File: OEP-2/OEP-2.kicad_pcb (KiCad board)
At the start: 2 copper layers, 50 x 25 mm, 7 parts, among them X1 Крепеж

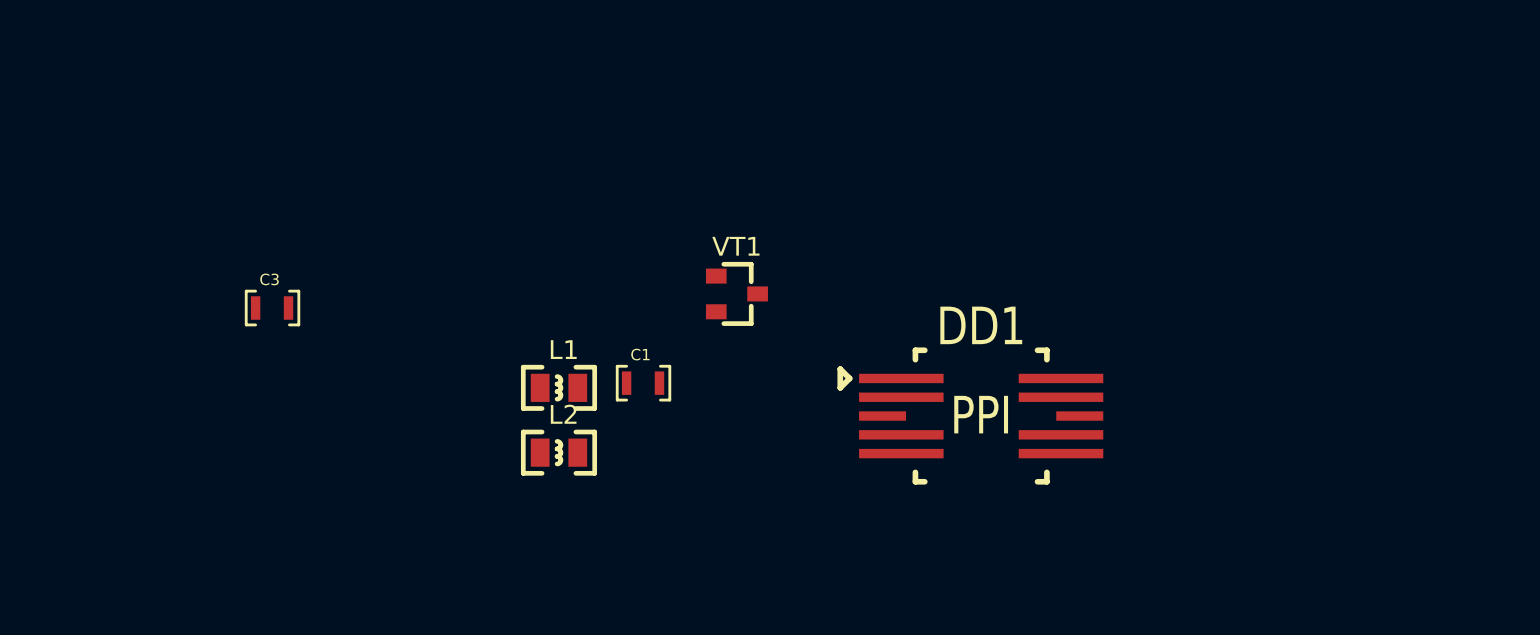
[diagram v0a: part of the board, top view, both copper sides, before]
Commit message: назначены посадочные места, кроме стабилитронов и  тантала
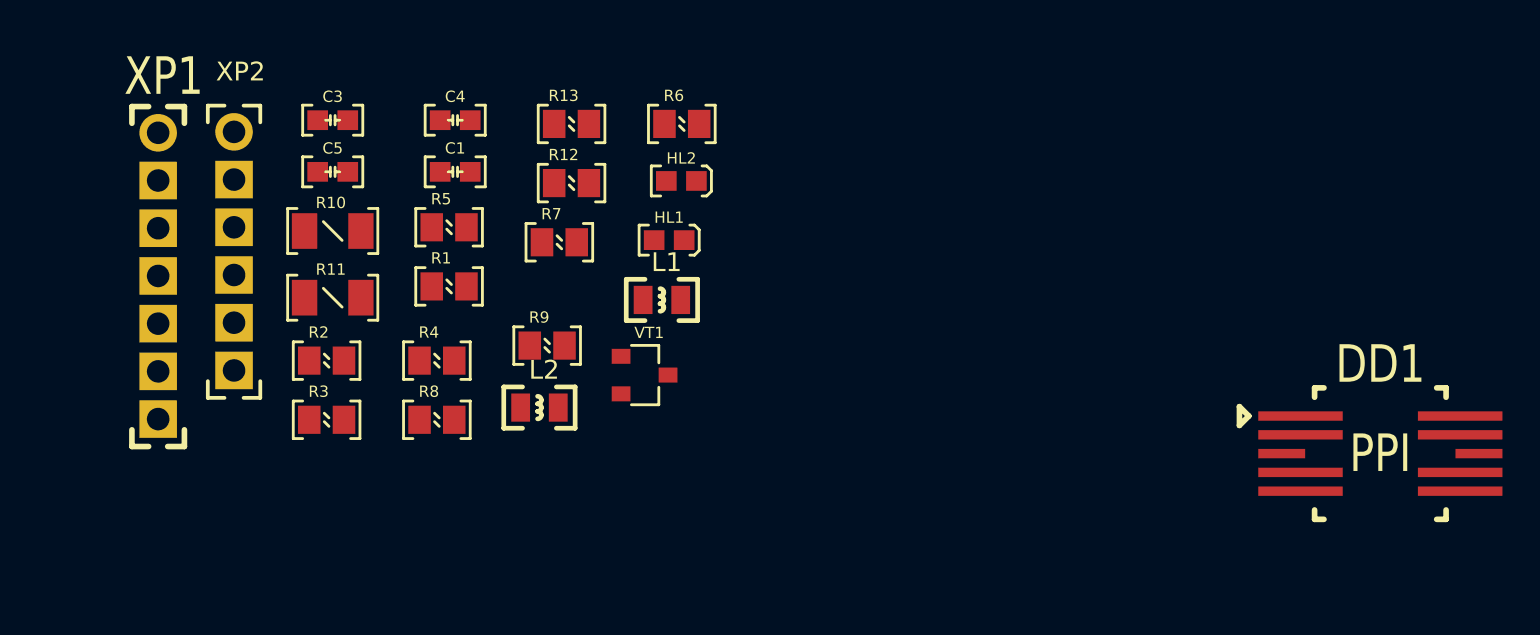
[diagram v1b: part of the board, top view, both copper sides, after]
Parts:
- added C4: Конденсатор_керамический, MOTOR_RLC:Конденсатор_SMD_IEC_0603, F.Cu at (103.8, 17.8)
- added C5: Конденсатор_керамический, MOTOR_RLC:Конденсатор_SMD_IEC_0603, F.Cu at (97.2, 20.5)
- added HL1: Светодиод, MOTOR_VD_VT_HL:Светодиод_SMD_IEC_0603, F.Cu at (115.1, 24.1)
- added HL2: Светодиод, MOTOR_VD_VT_HL:Светодиод_SMD_IEC_0603, F.Cu at (115.8, 21.0)
- added R1: Резистор_0,125Вт, MOTOR_RLC:Резистор_SMD_IEC_0805_0,125_Вт, F.Cu at (102.5, 26.6)
- added R10: Резистор_0,25Вт, MOTOR_RLC:Резистор_SMD_IEC_1206-0,25_Вт, F.Cu at (95.7, 23.6)
- added R11: Резистор_0,25Вт, MOTOR_RLC:Резистор_SMD_IEC_1206-0,25_Вт, F.Cu at (95.7, 27.2)
- added R12: Резистор_0,125Вт, MOTOR_RLC:Резистор_SMD_IEC_0805_0,125_Вт, F.Cu at (109.0, 21.1)
- added R13: Резистор_0,125Вт, MOTOR_RLC:Резистор_SMD_IEC_0805_0,125_Вт, F.Cu at (109.0, 17.9)
- added R2: Резистор_0,125Вт, MOTOR_RLC:Резистор_SMD_IEC_0805_0,125_Вт, F.Cu at (96.0, 30.6)
- added R3: Резистор_0,125Вт, MOTOR_RLC:Резистор_SMD_IEC_0805_0,125_Вт, F.Cu at (96.0, 33.7)
- added R4: Резистор_0,125Вт, MOTOR_RLC:Резистор_SMD_IEC_0805_0,125_Вт, F.Cu at (101.8, 30.6)
- added R5: Резистор_0,125Вт, MOTOR_RLC:Резистор_SMD_IEC_0805_0,125_Вт, F.Cu at (102.5, 23.4)
- added R6: Резистор_0,125Вт, MOTOR_RLC:Резистор_SMD_IEC_0805_0,125_Вт, F.Cu at (114.9, 17.9)
- added R7: Резистор_0,125Вт, MOTOR_RLC:Резистор_SMD_IEC_0805_0,125_Вт, F.Cu at (108.4, 24.2)
- added R8: Резистор_0,125Вт, MOTOR_RLC:Резистор_SMD_IEC_0805_0,125_Вт, F.Cu at (101.8, 33.7)
- added R9: Резистор_0,125Вт, MOTOR_RLC:Резистор_SMD_IEC_0805_0,125_Вт, F.Cu at (107.7, 29.8)
- added XP1: Вилка_СНП346-7ВП21-1#0, MOTOR_X:Вилка_СНП346-7ВП21-1-В, F.Cu at (87.9, 18.4)
- added XP2: Вилка_СНП346-6ВП21-1#1N1N6, MOTOR_X:Вилка_СНП346-6ВП21-1-В, F.Cu at (92.0, 18.4)
- C1, C3: footprint N_RLC:Конденсатор_SMD_0603_pnp -> MOTOR_RLC:Конденсатор_SMD_IEC_0603
- VT1: footprint N_VD_HL:Транзистор_IRLML6344TR_SOT-23 -> MOTOR_VD_VT_HL:Корпус_КТ-46
- moved DD1 21.3 mm to (151.0, 39.0)
- moved C1 15.1 mm to (103.8, 20.5)
- moved C3 10.5 mm to (97.2, 17.8)
- moved L1 7.21 mm to (113.8, 27.3)
- moved VT1 6.55 mm to (113.8, 31.3)
- moved L2 2.62 mm to (107.2, 33.0)
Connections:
- C3 pad 2: (no net) -> Net-(C3-Pad2)
- DD1 pad 1: (no net) -> /RX-RS
- DD1 pad 4: (no net) -> /TX-RS
- DD1 pad 7: (no net) -> /RS-B
- L1 pad 2: (no net) -> Net-(L1-Pad2)
- L2 pad 2: (no net) -> Net-(L2-Pad2)
- VT1 pad 1: (no net) -> Net-(R7-Pad1)
- X1 pad 1: (no net) -> Net-(X1-Pad1)

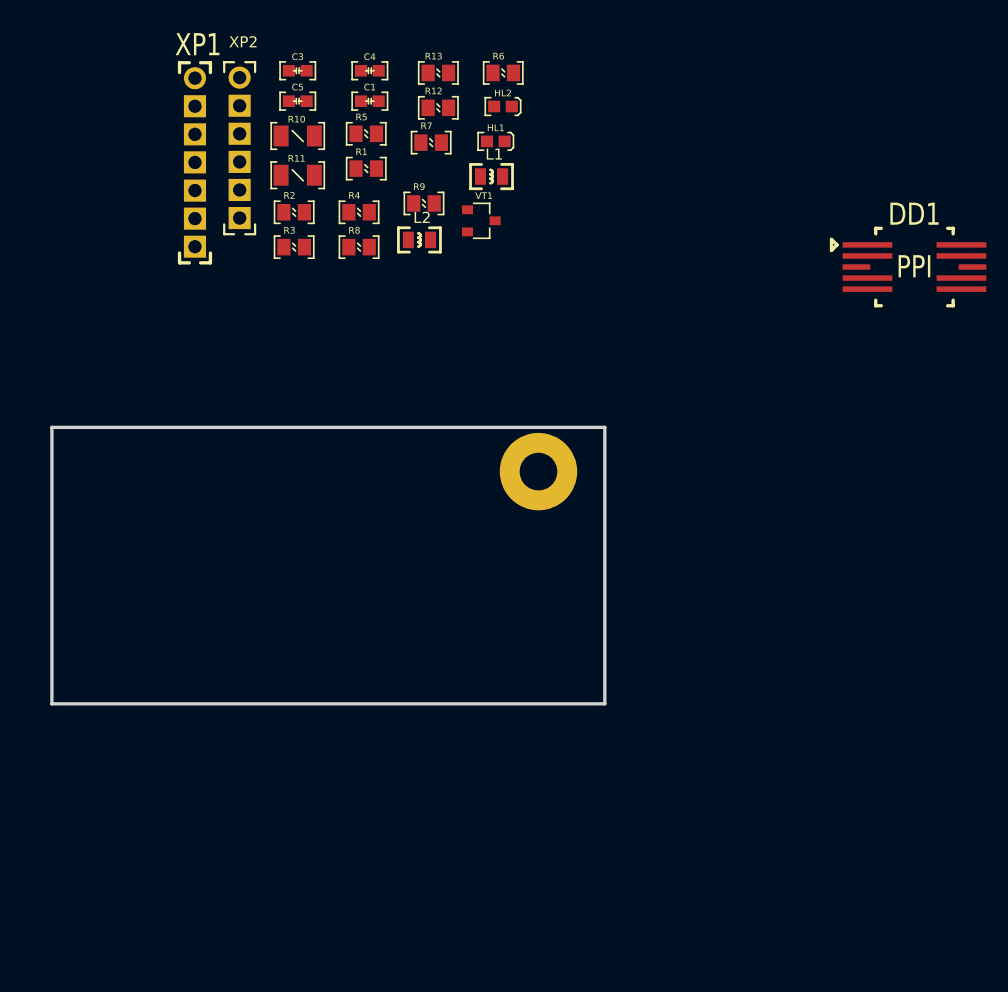
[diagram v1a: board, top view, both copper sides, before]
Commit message: назначены все посадочные места, готов сегмент  линий RS
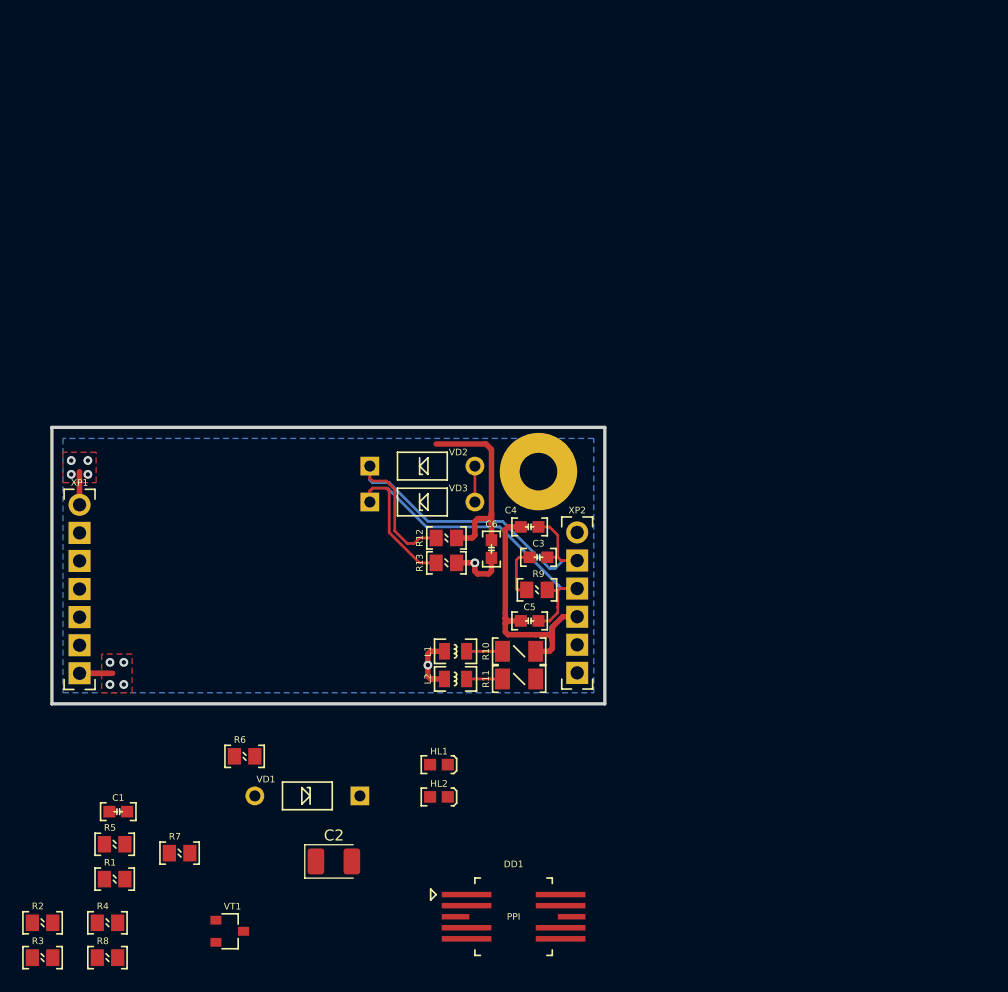
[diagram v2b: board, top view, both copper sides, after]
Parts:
- added C2: Конденсатор_электролитический, Capacitor_Tantalum_SMD:CP_EIA-3528-21_Kemet-B_Pad1.50x2.35mm_HandSolder, F.Cu at (100.5, 89.2)
- added C6: Конденсатор_керамический, N_RLC:Конденсатор_SMD_IEC_0603, F.Cu at (114.8, 61.0)
- added VD1: Стабилитрон_КС168В2, N_VD_HL:Стабилитрон_корпус_КД-2_в_отверстие, F.Cu at (93.3, 83.3)
- added VD2: Стабилитрон_КС168В2, N_VD_HL:Стабилитрон_корпус_КД-2_в_отверстие, F.Cu at (113.2, 53.5)
- added VD3: Стабилитрон_КС168В2, N_VD_HL:Стабилитрон_корпус_КД-2_в_отверстие, F.Cu at (113.2, 56.8)
- C1, C3, C4, C5: footprint MOTOR_RLC:Конденсатор_SMD_IEC_0603 -> N_RLC:Конденсатор_SMD_IEC_0603
- HL1, HL2: footprint MOTOR_VD_VT_HL:Светодиод_SMD_IEC_0603 -> N_VD_HL:Светодиод_SMD_IEC_0603
- moved DD1 69.0 mm to (114.8, 97.8)
- moved C1 68.2 mm to (81.0, 84.8)
- moved R1 68.2 mm to (79.8, 90.8)
- moved R2 68.2 mm to (73.2, 94.8)
- moved R3 68.2 mm to (73.2, 98.0)
- moved R4 68.2 mm to (79.1, 94.8)
- moved R5 68.2 mm to (79.8, 87.7)
- moved R7 68.2 mm to (85.6, 88.5)
- moved R8 68.2 mm to (79.1, 98.0)
- moved VT1 68.2 mm to (91.1, 95.6)
- moved R6 66.1 mm to (91.5, 79.8)
- moved HL2 62.7 mm to (110.0, 83.4)
- moved HL1 56.6 mm to (110.0, 80.5)
- moved C5 51.5 mm to (118.2, 67.5), turned to 180 degrees
- moved XP2 51.2 mm to (122.5, 59.5)
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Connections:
- X1 pad 1: Net-(X1-Pad1) -> (no net)
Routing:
- net /RS-B: track 0.00 -> 42.9 mm
- net /RS-A: track 0.00 -> 42.5 mm
- net /RS-C: track 0.00 -> 24.4 mm
- net 5V: track 0.00 -> 19.2 mm
- net GND: track 0.00 -> 19.0 mm, vias 0 -> 10
- net Net-(C3-Pad2): track 0.00 -> 4.68 mm
- net Net-(VD2-PadA): track 0.00 -> 3.25 mm
- net Net-(L2-Pad2): track 0.00 -> 3.25 mm
- net Net-(L1-Pad2): track 0.00 -> 3.25 mm
- added copper zone on B.Cu, net GND
- added copper zone on F.Cu, net GND
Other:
- net class PWR added: clearance 0.2, trace_width 0.5, via_dia 0.8, via_drill 0.4

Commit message: готова трассировка, подготовлены GBR
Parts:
- moved R8 44.6 mm to (95.5, 56.5), turned to 270 degrees
- moved VT1 40.8 mm to (89.8, 54.8)
- moved R3 37.9 mm to (90.6, 64.2), turned to 180 degrees
- moved R2 37.1 mm to (90.6, 62.0), turned to 180 degrees
- moved R7 34.8 mm to (84.0, 53.8), turned to 270 degrees
- moved R1 32.9 mm to (90.6, 59.8), turned to 180 degrees
- moved VD1 32.3 mm to (81.0, 53.5), turned to 270 degrees
- moved C2 32.3 mm to (84.2, 61.4), turned to 90 degrees
- moved C1 32.2 mm to (97.8, 57.3), turned to 270 degrees
- moved DD1 31.9 mm to (104.8, 67.5), turned to 90 degrees
- moved HL1 30.7 mm to (89.7, 57.5), turned to 180 degrees
- moved R4 30.5 mm to (90.6, 66.5), turned to 180 degrees
- moved HL2 22.7 mm to (89.7, 73.2), turned to 180 degrees
- moved R5 21.8 mm to (90.6, 68.8), turned to 180 degrees
- moved R6 8.80 mm to (90.6, 71.0), turned to 180 degrees
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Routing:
- net 5V: track 19.2 -> 76.0 mm
- net /EN-RS: track 0.00 -> 38.3 mm, vias 0 -> 2
- net /RX-RS: track 0.00 -> 29.8 mm, vias 0 -> 2
- net /TX-RS: track 0.00 -> 28.3 mm
- net /RX-MC: track 0.00 -> 21.3 mm
- net /TX-MC: track 0.00 -> 20.2 mm
- net GND: track 19.0 -> 34.6 mm, vias 10 -> 15
- net /EN-MC: track 0.00 -> 13.7 mm
- net /RS-A: track 42.5 -> 51.6 mm
- net /SHLD: track 0.00 -> 8.74 mm
- net /RS-B: track 42.9 -> 50.4 mm, vias 0 -> 1
- net Net-(R7-Pad1): track 0.00 -> 7.45 mm, vias 0 -> 2
- net Net-(HL2-PadA): track 0.00 -> 4.21 mm
- net Net-(HL1-PadA): track 0.00 -> 4.21 mm
- net /RS-C: track 24.4 -> 25.3 mm
- added copper zone on F.Cu, net 5V
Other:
- board text added: "OEP-2-0N7"
- board text added: "RX1"
- board text added: "RX2"
- board text added: "TX1"
- board text added: "TX2"
